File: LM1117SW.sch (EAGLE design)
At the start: 10 parts

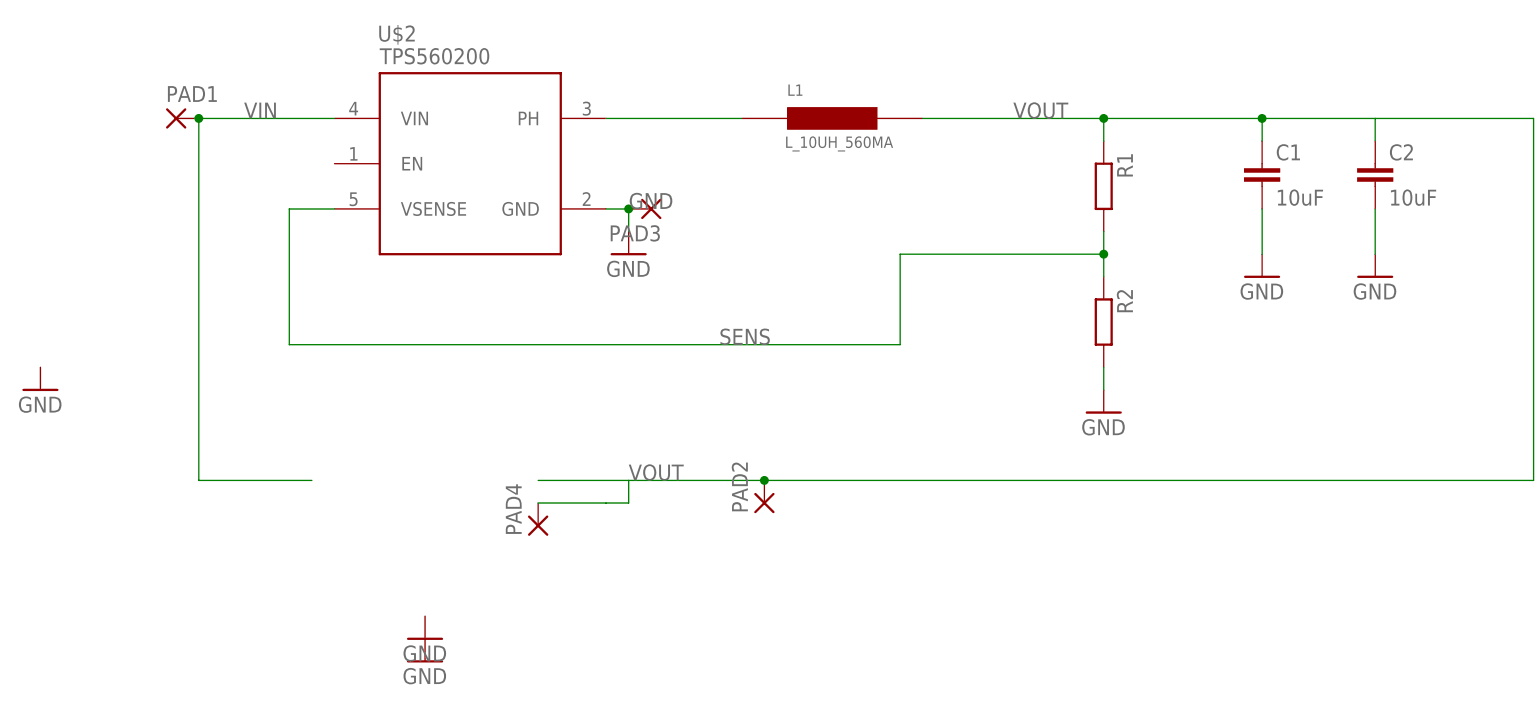
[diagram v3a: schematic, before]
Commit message: updated order list
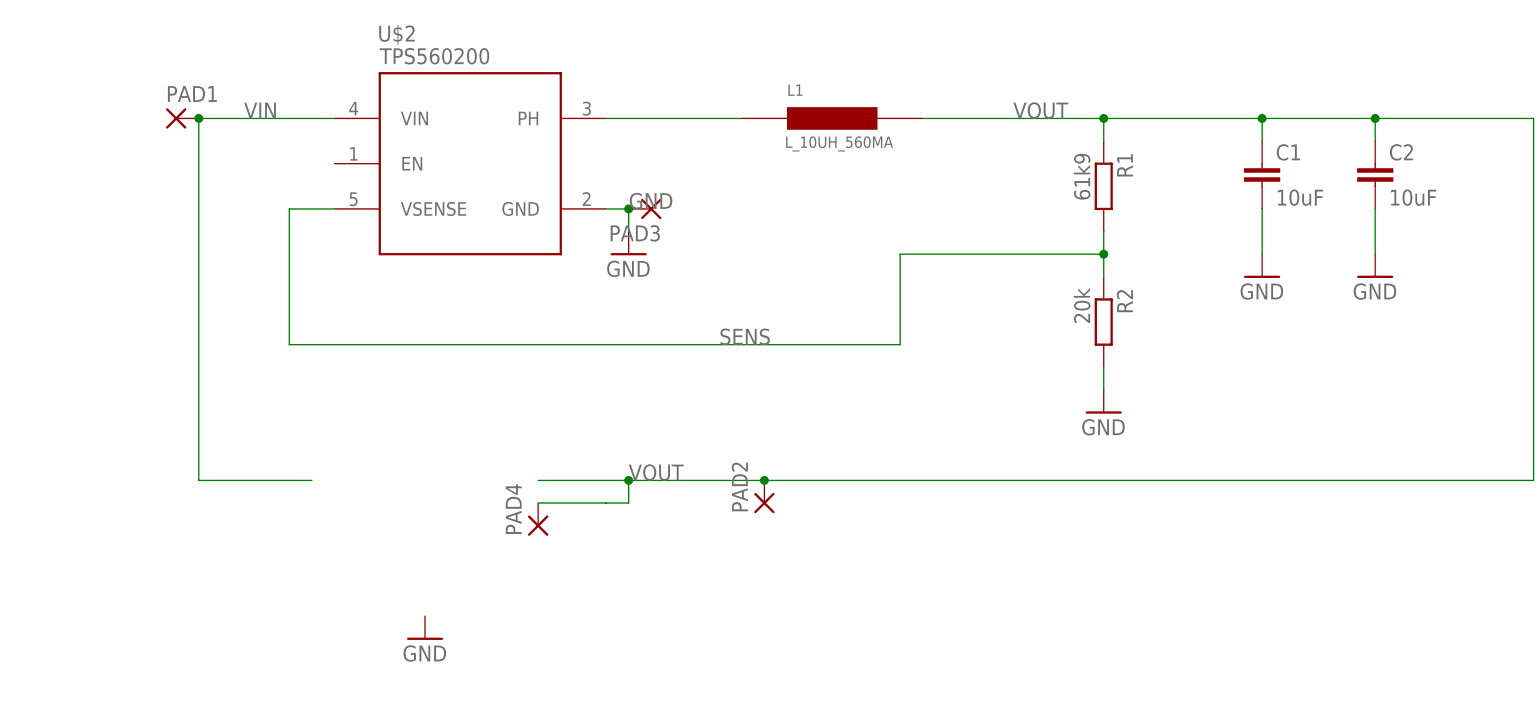
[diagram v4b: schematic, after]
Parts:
- C1, C2: MF (none) -> MULTICOMP; MPN (none) -> MC0805X106K250CT; OC_FARNELL 1759421 -> 2320833
- L1: MF (none) -> LAIRD TECHNOLOGIES; MPN (none) -> TYS3010100M-10; OC_FARNELL (none) -> 2292503
- PAD1, PAD2, PAD3, PAD4: OC_FARNELL (none) -> unknown
- R1: value (none) -> 61k9; MF (none) -> MULTICOMP; MPN (none) -> MC00625W0402161K9; OC_FARNELL (none) -> 1803730
- R2: value (none) -> 20k; MF (none) -> VISHAY DRALORIC; MPN (none) -> CRCW040220K0FKED; OC_FARNELL (none) -> 1469693
- U$2: MF (none) -> TEXAS INSTRUMENTS; MPN (none) -> TPS560200DBVT; OC_FARNELL (none) -> 2373566
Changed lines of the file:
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@@
 </classes>
 <parts>
-<part name="L1" library="Fabian" deviceset="L_10UH_560MA" device=""/>
-<part name="U$2" library="Fabian" deviceset="TPS560200" device=""/>
-<part name="R1" library="rcl" deviceset="R-EU_" device="R0402"/>
-<part name="R2" library="rcl" deviceset="R-EU_" device="R0402"/>
+<part name="L1" library="Fabian" deviceset="L_10UH_560MA" device="">
+<attribute name="MF" value="LAIRD TECHNOLOGIES"/>
+<attribute name="MPN" value="TYS3010100M-10"/>
+<attribute name="OC_FARNELL" value="2292503"/>
+</part>
+<part name="U$2" library="Fabian" deviceset="TPS560200" device="">
+<attribute name="MF" value="TEXAS INSTRUMENTS"/>
+<attribute name="MPN" value="TPS560200DBVT"/>
+<attribute name="OC_FARNELL" value="2373566"/>
+</part>
+<part name="R1" library="rcl" deviceset="R-EU_" device="R0402" value="61k9">
+<attribute name="MF" value="MULTICOMP"/>
+<attribute name="MPN" value="MC00625W0402161K9"/>
+<attribute name="OC_FARNELL" value="1803730"/>
+</part>
+<part name="R2" library="rcl" deviceset="R-EU_" device="R0402" value="20k">
+<attribute name="MF" value="VISHAY DRALORIC"/>
+<attribute name="MPN" value="CRCW040220K0FKED"/>
+<attribute name="OC_FARNELL" value="1469693"/>
+</part>
 <part name="C1" library="rcl" deviceset="C-EU" device="C0805K" value="10uF">
-<attribute name="OC_FARNELL" value="1759421"/>
+<attribute name="MF" value="MULTICOMP"/>
+<attribute name="MPN" value="MC0805X106K250CT"/>
+<attribute name="OC_FARNELL" value="2320833"/>
 </part>
 <part name="C2" library="rcl" deviceset="C-EU" device="C0805K" value="10uF">
-<attribute name="OC_FARNELL" value="1759421"/>
+<attribute name="MF" value="MULTICOMP"/>
+<attribute name="MPN" value="MC0805X106K250CT"/>
+<attribute name="OC_FARNELL" value="2320833"/>
 </part>
 <part name="GND1" library="supply1" deviceset="GND" device=""/>
@@
 <part name="GND3" library="supply1" deviceset="GND" device=""/>
 <part name="GND4" library="supply1" deviceset="GND" device=""/>
-<part name="GND5" library="supply1" deviceset="GND" device=""/>
-<part name="GND6" library="supply1" deviceset="GND" device=""/>
 <part name="GND7" library="supply1" deviceset="GND" device=""/>
-<part name="PAD1" library="wirepad" deviceset="1,6/0,9" device=""/>
-<part name="PAD2" library="wirepad" deviceset="1,6/0,9" device=""/>
-<part name="PAD3" library="wirepad" deviceset="1,6/0,9" device=""/>
-<part name="PAD4" library="wirepad" deviceset="1,6/0,9" device=""/>
+<part name="PAD1" library="wirepad" deviceset="1,6/0,9" device="">
+<attribute name="MF" value=""/>
+<attribute name="MPN" value=""/>
+<attribute name="OC_FARNELL" value="unknown"/>
+</part>
+<part name="PAD2" library="wirepad" deviceset="1,6/0,9" device="">
+<attribute name="MF" value=""/>
+<attribute name="MPN" value=""/>
+<attribute name="OC_FARNELL" value="unknown"/>
+</part>
+<part name="PAD3" library="wirepad" deviceset="1,6/0,9" device="">
+<attribute name="MF" value=""/>
+<attribute name="MPN" value=""/>
+<attribute name="OC_FARNELL" value="unknown"/>
+</part>
+<part name="PAD4" library="wirepad" deviceset="1,6/0,9" device="">
+<attribute name="MF" value=""/>
+<attribute name="MPN" value=""/>
+<attribute name="OC_FARNELL" value="unknown"/>
+</part>
 </parts>
 <sheets>
@@
 </plain>
 <instances>
-<instance part="L1" gate="G$1" x="78.74" y="66.04"/>
-<instance part="U$2" gate="G$1" x="38.1" y="60.96"/>
-<instance part="R1" gate="G$1" x="109.22" y="58.42" rot="R270"/>
-<instance part="R2" gate="G$1" x="109.22" y="43.18" rot="R270"/>
+<instance part="L1" gate="G$1" x="78.74" y="66.04">
+<attribute name="OC_FARNELL" x="78.74" y="66.04" size="1.778" layer="96" display="off"/>
+<attribute name="MF" x="78.74" y="66.04" size="1.778" layer="96" display="off"/>
+<attribute name="MPN" x="78.74" y="66.04" size="1.778" layer="96" display="off"/>
+</instance>
+<instance part="U$2" gate="G$1" x="38.1" y="60.96">
+<attribute name="OC_FARNELL" x="38.1" y="60.96" size="1.778" layer="96" display="off"/>
+<attribute name="MF" x="38.1" y="60.96" size="1.778" layer="96" display="off"/>
+<attribute name="MPN" x="38.1" y="60.96" size="1.778" layer="96" display="off"/>
+</instance>
+<instance part="R1" gate="G$1" x="109.22" y="58.42" rot="R270">
+<attribute name="OC_FARNELL" x="109.22" y="58.42" size="1.778" layer="96" display="off"/>
+<attribute name="MF" x="109.22" y="58.42" size="1.778" layer="96" display="off"/>
+<attribute name="MPN" x="109.22" y="58.42" size="1.778" layer="96" display="off"/>
+</instance>
+<instance part="R2" gate="G$1" x="109.22" y="43.18" rot="R270">
+<attribute name="OC_FARNELL" x="109.22" y="43.18" size="1.778" layer="96" display="off"/>
+<attribute name="MF" x="109.22" y="43.18" size="1.778" layer="96" display="off"/>
+<attribute name="MPN" x="109.22" y="43.18" size="1.778" layer="96" display="off"/>
+</instance>
 <instance part="C1" gate="G$1" x="127" y="60.96">
 <attribute name="OC_FARNELL" x="127" y="60.96" size="1.778" layer="96" display="off"/>
+<attribute name="MF" x="127" y="60.96" size="1.778" layer="96" display="off"/>
+<attribute name="MPN" x="127" y="60.96" size="1.778" layer="96" display="off"/>
 </instance>
 <instance part="C2" gate="G$1" x="139.7" y="60.96">
 <attribute name="OC_FARNELL" x="139.7" y="60.96" size="1.778" layer="96" display="off"/>
+<attribute name="MF" x="139.7" y="60.96" size="1.778" layer="96" display="off"/>
+<attribute name="MPN" x="139.7" y="60.96" size="1.778" layer="96" display="off"/>
 </instance>
 <instance part="GND1" gate="1" x="55.88" y="50.8"/>
@@
 <instance part="GND3" gate="1" x="127" y="48.26"/>
 <instance part="GND4" gate="1" x="139.7" y="48.26"/>
-<instance part="GND5" gate="1" x="-10.16" y="35.56"/>
-<instance part="GND6" gate="1" x="33.02" y="5.08"/>
 <instance part="GND7" gate="1" x="33.02" y="7.62"/>
-<instance part="PAD1" gate="1" x="5.08" y="66.04"/>
-<instance part="PAD2" gate="1" x="71.12" y="22.86" rot="R90"/>
-<instance part="PAD3" gate="1" x="58.42" y="55.88" rot="R180"/>
-<instance part="PAD4" gate="1" x="45.72" y="20.32" rot="R90"/>
+<instance part="PAD1" gate="1" x="5.08" y="66.04">
+<attribute name="OC_FARNELL" x="5.08" y="66.04" size="1.778" layer="96" display="off"/>
+<attribute name="MF" x="5.08" y="66.04" size="1.778" layer="96" display="off"/>
+<attribute name="MPN" x="5.08" y="66.04" size="1.778" layer="96" display="off"/>
+</instance>
+<instance part="PAD2" gate="1" x="71.12" y="22.86" rot="R90">
+<attribute name="OC_FARNELL" x="71.12" y="22.86" size="1.778" layer="96" display="off"/>
+<attribute name="MF" x="71.12" y="22.86" size="1.778" layer="96" display="off"/>
+<attribute name="MPN" x="71.12" y="22.86" size="1.778" layer="96" display="off"/>
+</instance>
+<instance part="PAD3" gate="1" x="58.42" y="55.88" rot="R180">
+<attribute name="OC_FARNELL" x="58.42" y="55.88" size="1.778" layer="96" display="off"/>
+<attribute name="MF" x="58.42" y="55.88" size="1.778" layer="96" display="off"/>
+<attribute name="MPN" x="58.42" y="55.88" size="1.778" layer="96" display="off"/>
+</instance>
+<instance part="PAD4" gate="1" x="45.72" y="20.32" rot="R90">
+<attribute name="OC_FARNELL" x="45.72" y="20.32" size="1.778" layer="96" display="off"/>
+<attribute name="MF" x="45.72" y="20.32" size="1.778" layer="96" display="off"/>
+<attribute name="MPN" x="45.72" y="20.32" size="1.778" layer="96" display="off"/>
+</instance>
 </instances>
 <busses>
@@
 <wire x1="53.34" y1="22.86" x2="55.88" y2="22.86" width="0.1524" layer="91"/>
 <wire x1="55.88" y1="22.86" x2="55.88" y2="25.4" width="0.1524" layer="91"/>
+<junction x="55.88" y="25.4"/>
+<junction x="139.7" y="66.04"/>
 </segment>
 </net>
